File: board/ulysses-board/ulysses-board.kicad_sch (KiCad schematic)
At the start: 1 part, among them J1 GPIO

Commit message: Make some minor fixes.
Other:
- sheet Alert & I2C IO renamed Status & I2C module
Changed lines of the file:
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@@
     (stroke (width 0.1524) (type solid) (color 0 0 0 0))
     (fill (color 0 0 0 0.0000))
-    (property "Sheet name" "Alert & I2C IO" (id 0) (at 142.24 85.6484 0)
+    (property "Sheet name" "Status & I2C module" (id 0) (at 142.24 85.6484 0)
       (effects (font (size 1.27 1.27)) (justify left bottom))
     )

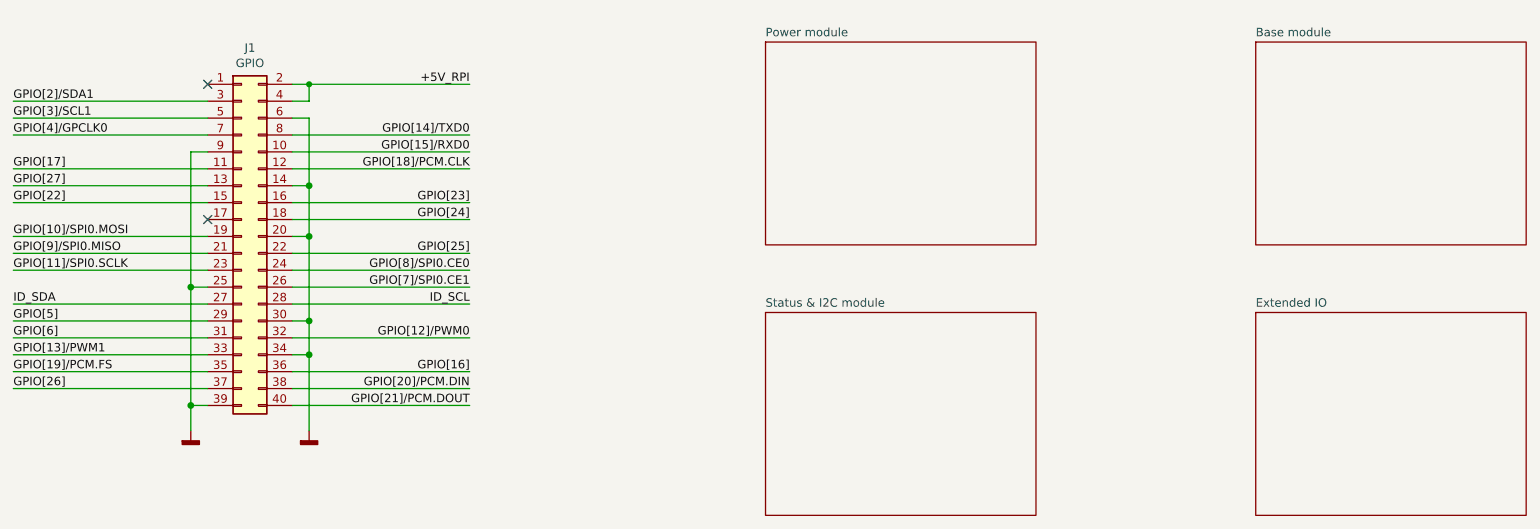
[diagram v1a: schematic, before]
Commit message: Add a real-time clock.
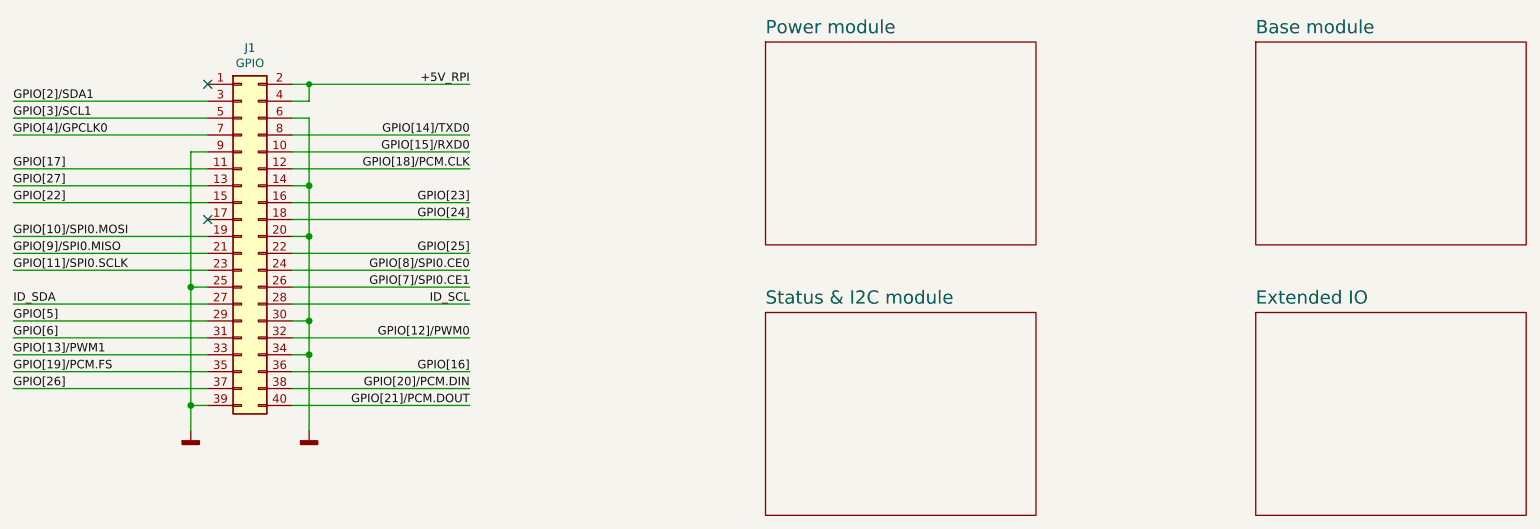
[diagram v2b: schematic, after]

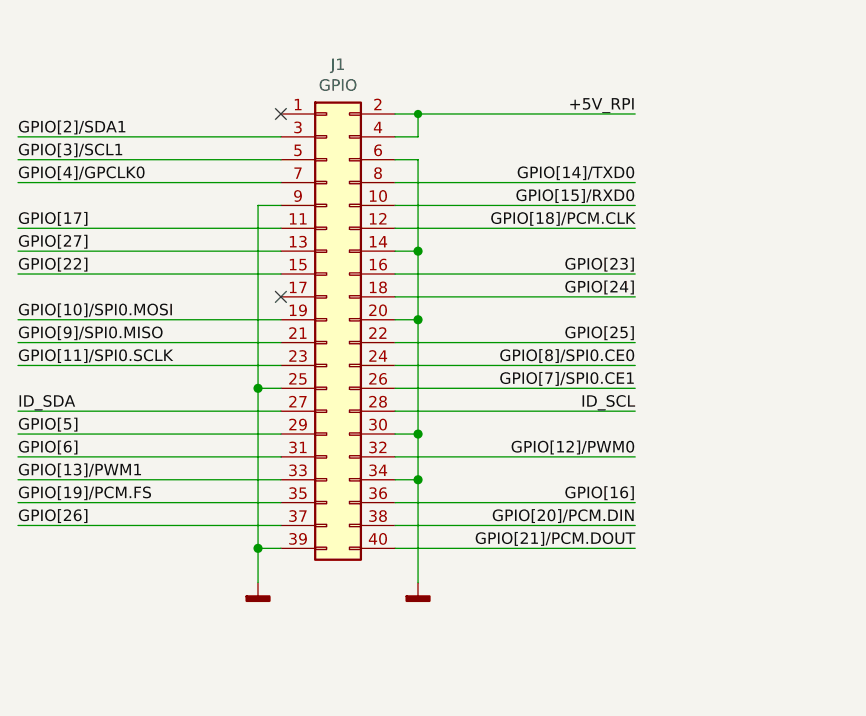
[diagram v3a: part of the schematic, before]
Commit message: Make schemaics more readable.
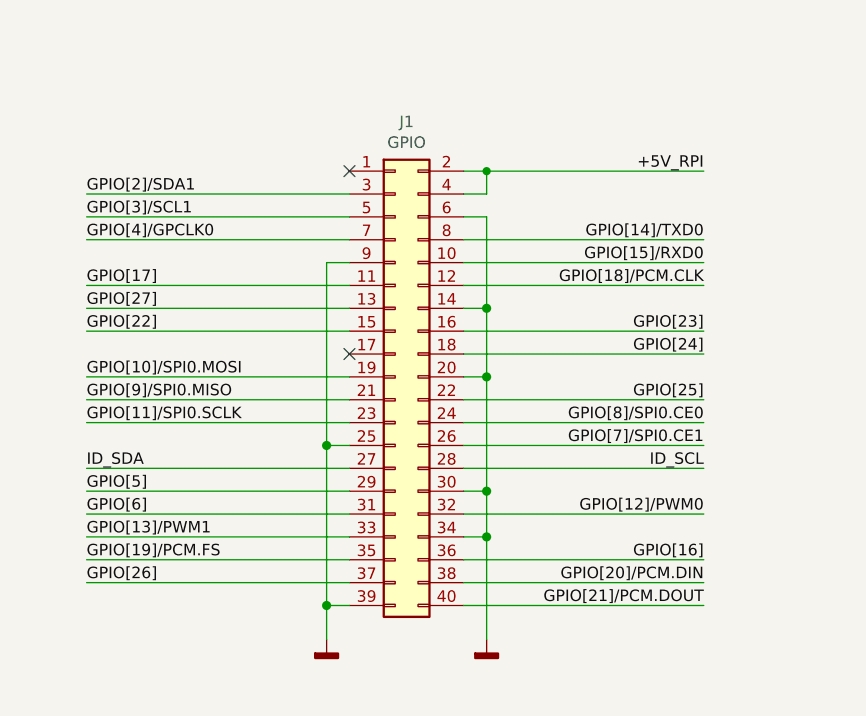
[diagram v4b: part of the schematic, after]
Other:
- moved on the sheet: J1
